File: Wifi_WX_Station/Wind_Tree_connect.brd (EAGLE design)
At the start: 25.5 x 25.5 mm, 4 parts, among them J1 RJ45-8VERT

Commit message: updated BOM with all prices- As Checked in to BATCH PCB
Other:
- board text added: "WIND_SPEED"
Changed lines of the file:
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@@
 <plain>
 <circle x="13.97" y="13.97" radius="12.763340625" width="0.0254" layer="20"/>
-<text x="17.78" y="22.225" size="1.016" layer="52" font="vector" rot="MR0">GND</text>
-<text x="15.24" y="10.795" size="1.016" layer="52" font="vector" rot="MR90">+5V</text>
+<text x="13.97" y="22.225" size="1.016" layer="52" font="vector" rot="MR0">GND</text>
+<text x="14.605" y="8.89" size="1.016" layer="52" font="vector" rot="MR0">+5V</text>
+<text x="22.704040625" y="18.75834375" size="1.27" layer="22" rot="MR270">WIND_SPEED</text>
 </plain>
 <attributes>
@@
 <element name="J1" library="wifi_WX" package="RJ45_VERT" value="RJ45-8VERT" x="8.255" y="12.065"/>
 <element name="WIND_DIR" library="wifi_WX" package="1X03" value="" x="3.81" y="13.97" smashed="yes" rot="MR90">
-<attribute name="NAME" x="5.6388" y="6.9088" size="1.27" layer="26" ratio="10" rot="MR90"/>
+<attribute name="NAME" x="5.45684375" y="8.667971875" size="1.27" layer="26" ratio="10" rot="MR90"/>
 <attribute name="VALUE" x="0.635" y="10.16" size="1.27" layer="28" rot="MR90"/>
 </element>
 <element name="WIND_COUNT" library="wifi_WX" package="1X03" value="" x="24.13" y="13.97" smashed="yes" rot="MR90">
-<attribute name="NAME" x="20.8788" y="6.9088" size="1.27" layer="26" ratio="10" rot="MR90"/>
 <attribute name="VALUE" x="20.955" y="10.16" size="1.27" layer="28" rot="MR90"/>
 </element>
-<element name="SUN" library="wifi_WX" package="1X03" value="" x="13.97" y="3.81" rot="MR0"/>
+<element name="SUN" library="wifi_WX" package="1X03" value="" x="13.97" y="3.81" smashed="yes" rot="MR0">
+<attribute name="NAME" x="15.3162" y="5.6388" size="1.27" layer="26" ratio="10" rot="MR0"/>
+<attribute name="VALUE" x="17.78" y="0.635" size="1.27" layer="28" rot="MR0"/>
+</element>
 </elements>
 <signals>

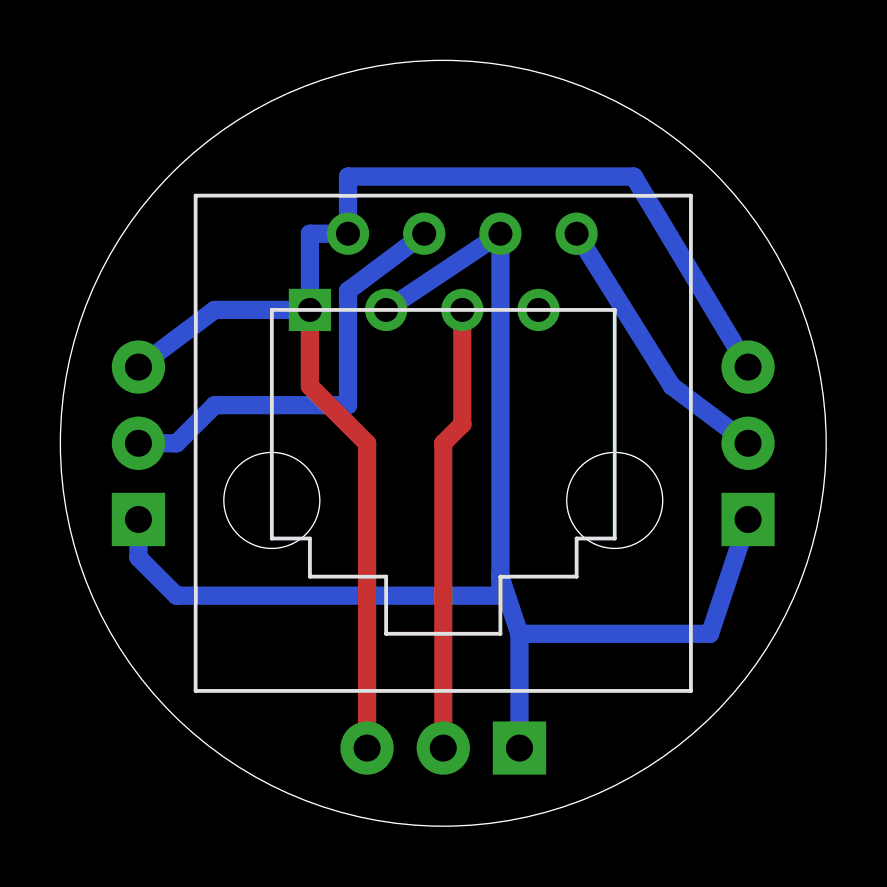
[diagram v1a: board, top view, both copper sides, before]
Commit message: 
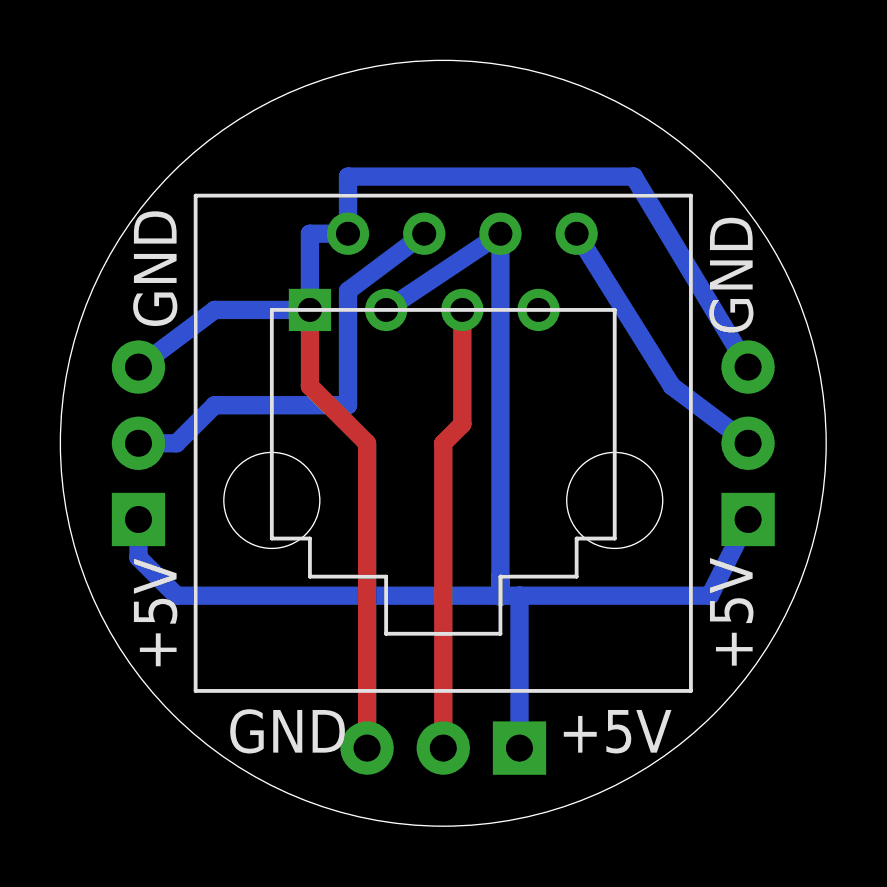
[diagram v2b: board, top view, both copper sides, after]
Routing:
- net +5V: track 46.7 -> 46.1 mm
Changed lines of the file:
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@@
 <setting verticaltext="up"/>
 </settings>
-<grid distance="0.05" unitdist="inch" unit="inch" style="lines" multiple="1" display="no" altdistance="0.003125" altunitdist="mic" altunit="mm"/>
+<grid distance="0.05" unitdist="inch" unit="inch" style="lines" multiple="1" display="no" altdistance="0.025" altunitdist="inch" altunit="inch"/>
 <layers>
 <layer number="1" name="Top" color="4" fill="1" visible="yes" active="yes"/>
@@
 <layer number="27" name="tValues" color="7" fill="1" visible="yes" active="yes"/>
 <layer number="28" name="bValues" color="7" fill="1" visible="yes" active="yes"/>
-<layer number="29" name="tStop" color="7" fill="3" visible="yes" active="yes"/>
-<layer number="30" name="bStop" color="7" fill="6" visible="yes" active="yes"/>
+<layer number="29" name="tStop" color="7" fill="3" visible="no" active="yes"/>
+<layer number="30" name="bStop" color="7" fill="6" visible="no" active="yes"/>
 <layer number="31" name="tCream" color="7" fill="4" visible="yes" active="yes"/>
 <layer number="32" name="bCream" color="7" fill="5" visible="yes" active="yes"/>
@@
 <plain>
 <circle x="13.97" y="13.97" radius="12.763340625" width="0.0254" layer="20"/>
-<text x="13.97" y="22.225" size="1.016" layer="52" font="vector" rot="MR0">GND</text>
-<text x="14.605" y="8.89" size="1.016" layer="52" font="vector" rot="MR0">+5V</text>
+<text x="12.7" y="23.495" size="1.4224" layer="22" font="vector" rot="MR180">GND</text>
 <text x="22.704040625" y="18.75834375" size="1.27" layer="22" rot="MR270">WIND_SPEED</text>
+<text x="5.08" y="6.35" size="1.4224" layer="21" font="vector" rot="R90">+5V</text>
+<text x="21.59" y="5.08" size="1.4224" layer="21" font="vector" rot="R180">+5V</text>
+<text x="5.08" y="17.78" size="1.4224" layer="21" font="vector" rot="R90">GND</text>
+<text x="16.9590125" y="8.440984375" size="1.4224" layer="22" font="vector" rot="MR0">+5V</text>
+<text x="10.795" y="5.08" size="1.4224" layer="21" font="vector" rot="R180">GND</text>
+<text x="22.86" y="21.59" size="1.4224" layer="21" font="vector" rot="R270">GND</text>
+<text x="22.86" y="10.16" size="1.4224" layer="21" font="vector" rot="R270">+5V</text>
 </plain>
 <attributes>
@@
 <element name="J1" library="wifi_WX" package="RJ45_VERT" value="RJ45-8VERT" x="8.255" y="12.065"/>
 <element name="WIND_DIR" library="wifi_WX" package="1X03" value="" x="3.81" y="13.97" smashed="yes" rot="MR90">
-<attribute name="NAME" x="5.45684375" y="8.667971875" size="1.27" layer="26" ratio="10" rot="MR90"/>
+<attribute name="NAME" x="5.45684375" y="7.397971875" size="1.27" layer="26" ratio="10" rot="MR90"/>
 <attribute name="VALUE" x="0.635" y="10.16" size="1.27" layer="28" rot="MR90"/>
 </element>
@@
 <wire x1="15.875" y1="20.955" x2="15.875" y2="9.525" width="0.6096" layer="16"/>
 <wire x1="15.875" y1="8.89" x2="15.875" y2="9.525" width="0.6096" layer="16"/>
-<wire x1="15.875" y1="9.525" x2="16.51" y2="7.62" width="0.6096" layer="16"/>
-<wire x1="16.51" y1="7.62" x2="16.51" y2="3.81" width="0.6096" layer="16"/>
-<wire x1="24.13" y1="11.43" x2="22.86" y2="7.62" width="0.6096" layer="16"/>
-<wire x1="22.86" y1="7.62" x2="16.51" y2="7.62" width="0.6096" layer="16"/>
+<wire x1="15.875" y1="9.525" x2="15.8787625" y2="8.8522125" width="0.6096" layer="16"/>
+<wire x1="15.8787625" y1="8.8522125" x2="15.8787625" y2="8.89" width="0.6096" layer="16"/>
+<wire x1="15.8787625" y1="8.89" x2="16.51" y2="8.89" width="0.6096" layer="16"/>
+<wire x1="16.51" y1="8.89" x2="16.51" y2="3.81" width="0.6096" layer="16"/>
+<wire x1="24.13" y1="11.43" x2="22.86" y2="8.89" width="0.6096" layer="16"/>
+<wire x1="22.86" y1="8.89" x2="16.51" y2="8.89" width="0.6096" layer="16"/>
 <wire x1="3.81" y1="11.43" x2="3.81" y2="10.16" width="0.6096" layer="16"/>
 <wire x1="3.81" y1="10.16" x2="5.08" y2="8.89" width="0.6096" layer="16"/>

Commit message: Added multiple new boards - H-pwrdist- Insp_Wind_enc, 5040 etc..
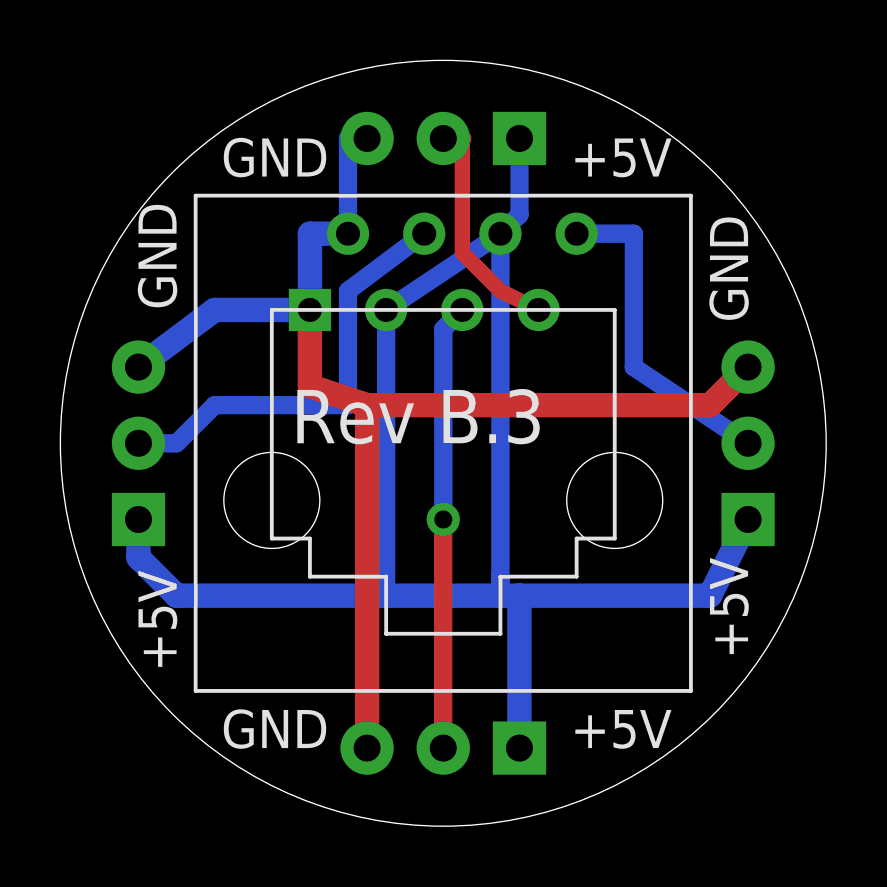
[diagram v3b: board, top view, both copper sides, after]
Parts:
- added RAIN: (no value), wifi_WX:1X03
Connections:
- net +5V: now also RAIN.1
- net GND: now also RAIN.3
- net RAIN_CNT_IN: now also RAIN.2
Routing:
- net +5V: track 46.1 -> 59.1 mm
- net RAIN_CNT_IN: track 0.00 -> 7.66 mm
- net WIND_COUNT_IN: track 9.17 -> 10.9 mm
- net GND: track 44.4 -> 43.2 mm
- net SUN_IN: vias 0 -> 1
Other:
- board text added: "Rev B.3"
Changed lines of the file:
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@@
 <plain>
 <circle x="13.97" y="13.97" radius="12.763340625" width="0.0254" layer="20"/>
-<text x="12.7" y="23.495" size="1.4224" layer="22" font="vector" rot="MR180">GND</text>
 <text x="22.704040625" y="18.75834375" size="1.27" layer="22" rot="MR270">WIND_SPEED</text>
-<text x="5.08" y="6.35" size="1.4224" layer="21" font="vector" rot="R90">+5V</text>
-<text x="21.59" y="5.08" size="1.4224" layer="21" font="vector" rot="R180">+5V</text>
-<text x="5.08" y="17.78" size="1.4224" layer="21" font="vector" rot="R90">GND</text>
-<text x="16.9590125" y="8.440984375" size="1.4224" layer="22" font="vector" rot="MR0">+5V</text>
-<text x="10.795" y="5.08" size="1.4224" layer="21" font="vector" rot="R180">GND</text>
-<text x="22.86" y="21.59" size="1.4224" layer="21" font="vector" rot="R270">GND</text>
-<text x="22.86" y="10.16" size="1.4224" layer="21" font="vector" rot="R270">+5V</text>
+<text x="5.08" y="6.35" size="1.27" layer="21" font="vector" rot="R90">+5V</text>
+<text x="21.59" y="5.08" size="1.27" layer="21" font="vector" rot="R180">+5V</text>
+<text x="5.08" y="18.415" size="1.27" layer="21" font="vector" rot="R90">GND</text>
+<text x="10.16" y="5.08" size="1.27" layer="21" font="vector" rot="R180">GND</text>
+<text x="22.86" y="21.59" size="1.27" layer="21" font="vector" rot="R270">GND</text>
+<text x="22.86" y="10.16" size="1.27" layer="21" font="vector" rot="R270">+5V</text>
+<text x="10.16" y="24.13" size="1.27" layer="21" font="vector" rot="R180">GND</text>
+<text x="21.59" y="24.13" size="1.27" layer="21" font="vector" rot="R180">+5V</text>
+<text x="8.89" y="13.97" size="1.778" layer="21" font="vector">Rev B.3</text>
 </plain>
 <attributes>
@@
 <attribute name="VALUE" x="17.78" y="0.635" size="1.27" layer="28" rot="MR0"/>
 </element>
+<element name="RAIN" library="wifi_WX" package="1X03" value="" x="13.97" y="24.13" smashed="yes" rot="MR0">
+<attribute name="NAME" x="22.3012" y="22.1488" size="1.27" layer="26" ratio="10" rot="MR0"/>
+<attribute name="VALUE" x="17.78" y="20.955" size="1.27" layer="28" rot="MR0"/>
+</element>
 </elements>
 <signals>
@@
 <contactref element="WIND_COUNT" pad="3"/>
 <contactref element="SUN" pad="3"/>
-<wire x1="3.81" y1="16.51" x2="6.35" y2="18.415" width="0.6096" layer="16"/>
-<wire x1="6.35" y1="18.415" x2="9.525" y2="18.415" width="0.6096" layer="16"/>
-<wire x1="9.525" y1="18.415" x2="9.525" y2="20.955" width="0.6096" layer="16"/>
-<wire x1="9.525" y1="20.955" x2="10.795" y2="20.955" width="0.6096" layer="16"/>
-<wire x1="10.795" y1="20.955" x2="10.795" y2="22.86" width="0.6096" layer="16"/>
-<wire x1="10.795" y1="22.86" x2="20.32" y2="22.86" width="0.6096" layer="16"/>
-<wire x1="20.32" y1="22.86" x2="24.13" y2="16.51" width="0.6096" layer="16"/>
-<wire x1="9.525" y1="18.415" x2="9.525" y2="15.875" width="0.6096" layer="1"/>
-<wire x1="9.525" y1="15.875" x2="11.43" y2="13.97" width="0.6096" layer="1"/>
-<wire x1="11.43" y1="13.97" x2="11.43" y2="3.81" width="0.6096" layer="1"/>
+<wire x1="3.81" y1="16.51" x2="6.35" y2="18.415" width="0.8128" layer="16"/>
+<wire x1="6.35" y1="18.415" x2="9.525" y2="18.415" width="0.8128" layer="16"/>
+<wire x1="9.525" y1="18.415" x2="9.525" y2="20.955" width="0.8128" layer="16"/>
+<wire x1="9.525" y1="20.955" x2="10.795" y2="20.955" width="0.8128" layer="16"/>
+<wire x1="9.525" y1="18.415" x2="9.525" y2="15.875" width="0.8128" layer="1"/>
+<wire x1="9.525" y1="15.875" x2="11.43" y2="15.24" width="0.8128" layer="1"/>
+<wire x1="11.43" y1="15.24" x2="11.43" y2="3.81" width="0.8128" layer="1"/>
+<contactref element="RAIN" pad="3"/>
+<wire x1="24.13" y1="16.51" x2="22.86" y2="15.24" width="0.8128" layer="1"/>
+<wire x1="22.86" y1="15.24" x2="11.43" y2="15.24" width="0.8128" layer="1"/>
+<wire x1="11.43" y1="24.13" x2="10.795" y2="24.13" width="0.6096" layer="16"/>
+<wire x1="10.795" y1="24.13" x2="10.795" y2="20.955" width="0.6096" layer="16"/>
 </signal>
 <signal name="+5V">
@@
 <wire x1="15.875" y1="9.525" x2="15.8787625" y2="8.8522125" width="0.6096" layer="16"/>
 <wire x1="15.8787625" y1="8.8522125" x2="15.8787625" y2="8.89" width="0.6096" layer="16"/>
-<wire x1="15.8787625" y1="8.89" x2="16.51" y2="8.89" width="0.6096" layer="16"/>
-<wire x1="16.51" y1="8.89" x2="16.51" y2="3.81" width="0.6096" layer="16"/>
-<wire x1="24.13" y1="11.43" x2="22.86" y2="8.89" width="0.6096" layer="16"/>
-<wire x1="22.86" y1="8.89" x2="16.51" y2="8.89" width="0.6096" layer="16"/>
-<wire x1="3.81" y1="11.43" x2="3.81" y2="10.16" width="0.6096" layer="16"/>
-<wire x1="3.81" y1="10.16" x2="5.08" y2="8.89" width="0.6096" layer="16"/>
-<wire x1="5.08" y1="8.89" x2="15.875" y2="8.89" width="0.6096" layer="16"/>
+<wire x1="15.8787625" y1="8.89" x2="16.51" y2="8.89" width="0.8128" layer="16"/>
+<wire x1="16.51" y1="8.89" x2="16.51" y2="3.81" width="0.8128" layer="16"/>
+<wire x1="24.13" y1="11.43" x2="22.86" y2="8.89" width="0.8128" layer="16"/>
+<wire x1="22.86" y1="8.89" x2="16.51" y2="8.89" width="0.8128" layer="16"/>
+<wire x1="3.81" y1="11.43" x2="3.81" y2="10.16" width="0.8128" layer="16"/>
+<wire x1="3.81" y1="10.16" x2="5.08" y2="8.89" width="0.8128" layer="16"/>
+<wire x1="5.08" y1="8.89" x2="12.065" y2="8.89" width="0.8128" layer="16"/>
+<wire x1="12.065" y1="8.89" x2="15.875" y2="8.89" width="0.8128" layer="16"/>
 <wire x1="15.875" y1="20.955" x2="12.065" y2="18.415" width="0.6096" layer="16"/>
+<contactref element="RAIN" pad="1"/>
+<wire x1="15.875" y1="20.955" x2="16.51" y2="21.59" width="0.6096" layer="16"/>
+<wire x1="12.065" y1="18.415" x2="12.065" y2="8.89" width="0.6096" layer="16"/>
+<wire x1="16.51" y1="24.13" x2="16.51" y2="21.59" width="0.6096" layer="16"/>
 </signal>
 <signal name="WIN_DIR_IN">
@@
 <contactref element="J1" pad="P$8"/>
 <contactref element="WIND_COUNT" pad="2"/>
-<wire x1="18.415" y1="20.955" x2="21.59" y2="15.875" width="0.6096" layer="16"/>
-<wire x1="21.59" y1="15.875" x2="24.13" y2="13.97" width="0.6096" layer="16"/>
+<wire x1="18.415" y1="20.955" x2="20.32" y2="20.955" width="0.6096" layer="16"/>
+<wire x1="20.32" y1="20.955" x2="20.32" y2="16.51" width="0.6096" layer="16"/>
+<wire x1="24.13" y1="13.97" x2="20.32" y2="16.51" width="0.6096" layer="16"/>
 </signal>
 <signal name="SUN_IN">
 <contactref element="J1" pad="P$5"/>
 <contactref element="SUN" pad="2"/>
-<wire x1="14.605" y1="18.415" x2="14.605" y2="14.605" width="0.6096" layer="1"/>
-<wire x1="14.605" y1="14.605" x2="13.97" y2="13.97" width="0.6096" layer="1"/>
-<wire x1="13.97" y1="13.97" x2="13.97" y2="3.81" width="0.6096" layer="1"/>
+<wire x1="13.97" y1="3.81" x2="13.97" y2="11.43" width="0.6096" layer="1"/>
+<via x="13.97" y="11.43" extent="1-16" drill="0.6" shape="square"/>
+<wire x1="13.97" y1="11.43" x2="13.97" y2="17.78" width="0.6096" layer="16"/>
+<wire x1="13.97" y1="17.78" x2="14.605" y2="18.415" width="0.6096" layer="16"/>
 </signal>
 <signal name="RAIN_CNT_IN">
 <contactref element="J1" pad="P$7"/>
+<contactref element="RAIN" pad="2"/>
+<wire x1="14.605" y1="24.13" x2="14.605" y2="20.32" width="0.508" layer="1"/>
+<wire x1="14.605" y1="20.32" x2="15.875" y2="19.05" width="0.508" layer="1"/>
+<wire x1="15.875" y1="19.05" x2="17.145" y2="18.415" width="0.508" layer="1"/>
+<wire x1="13.97" y1="24.13" x2="14.605" y2="24.13" width="0.6096" layer="1"/>
 </signal>
 </signals>
